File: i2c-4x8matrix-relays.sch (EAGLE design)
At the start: 83 parts, among them IC1 MCP23008/SS, IC2 MCP23008/SS, IC3 MCP23008/SS, IC4 MCP23008/SS, IC5 TBD62083AFNG, IC6 TBD62083AFNG, IC7 TBD62083AFNG, IC8 TBD62083AFNG

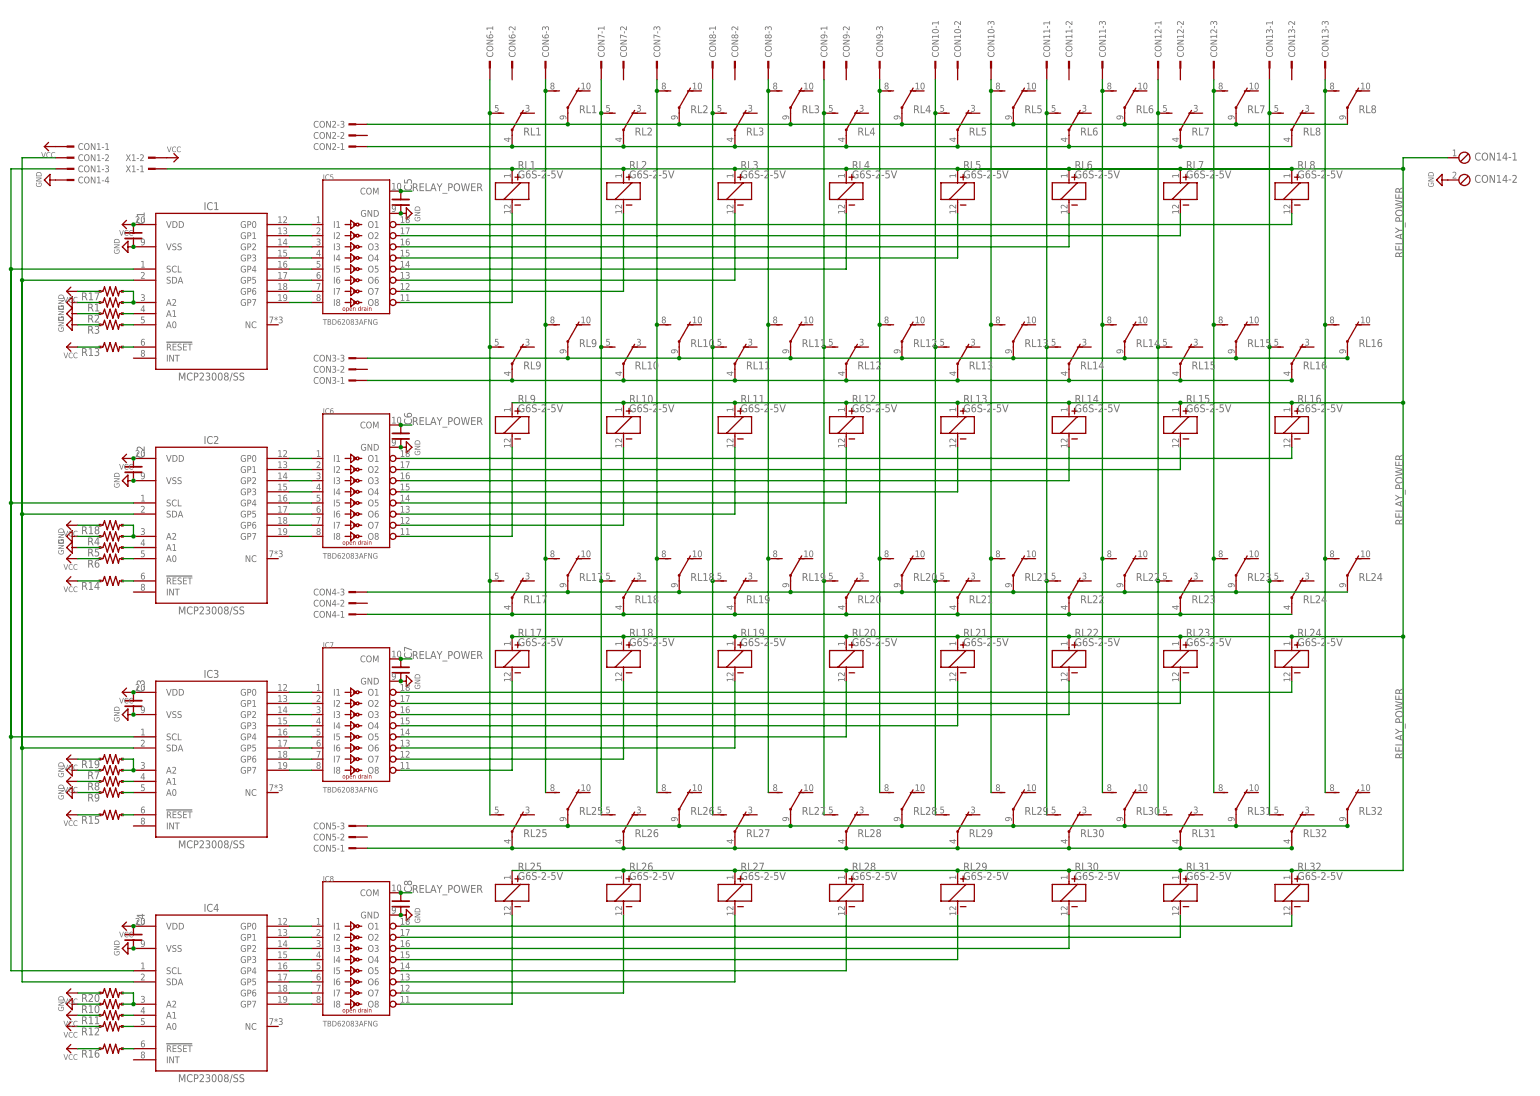
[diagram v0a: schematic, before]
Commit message: update schematic and layout to use PCA9XXX IO expander
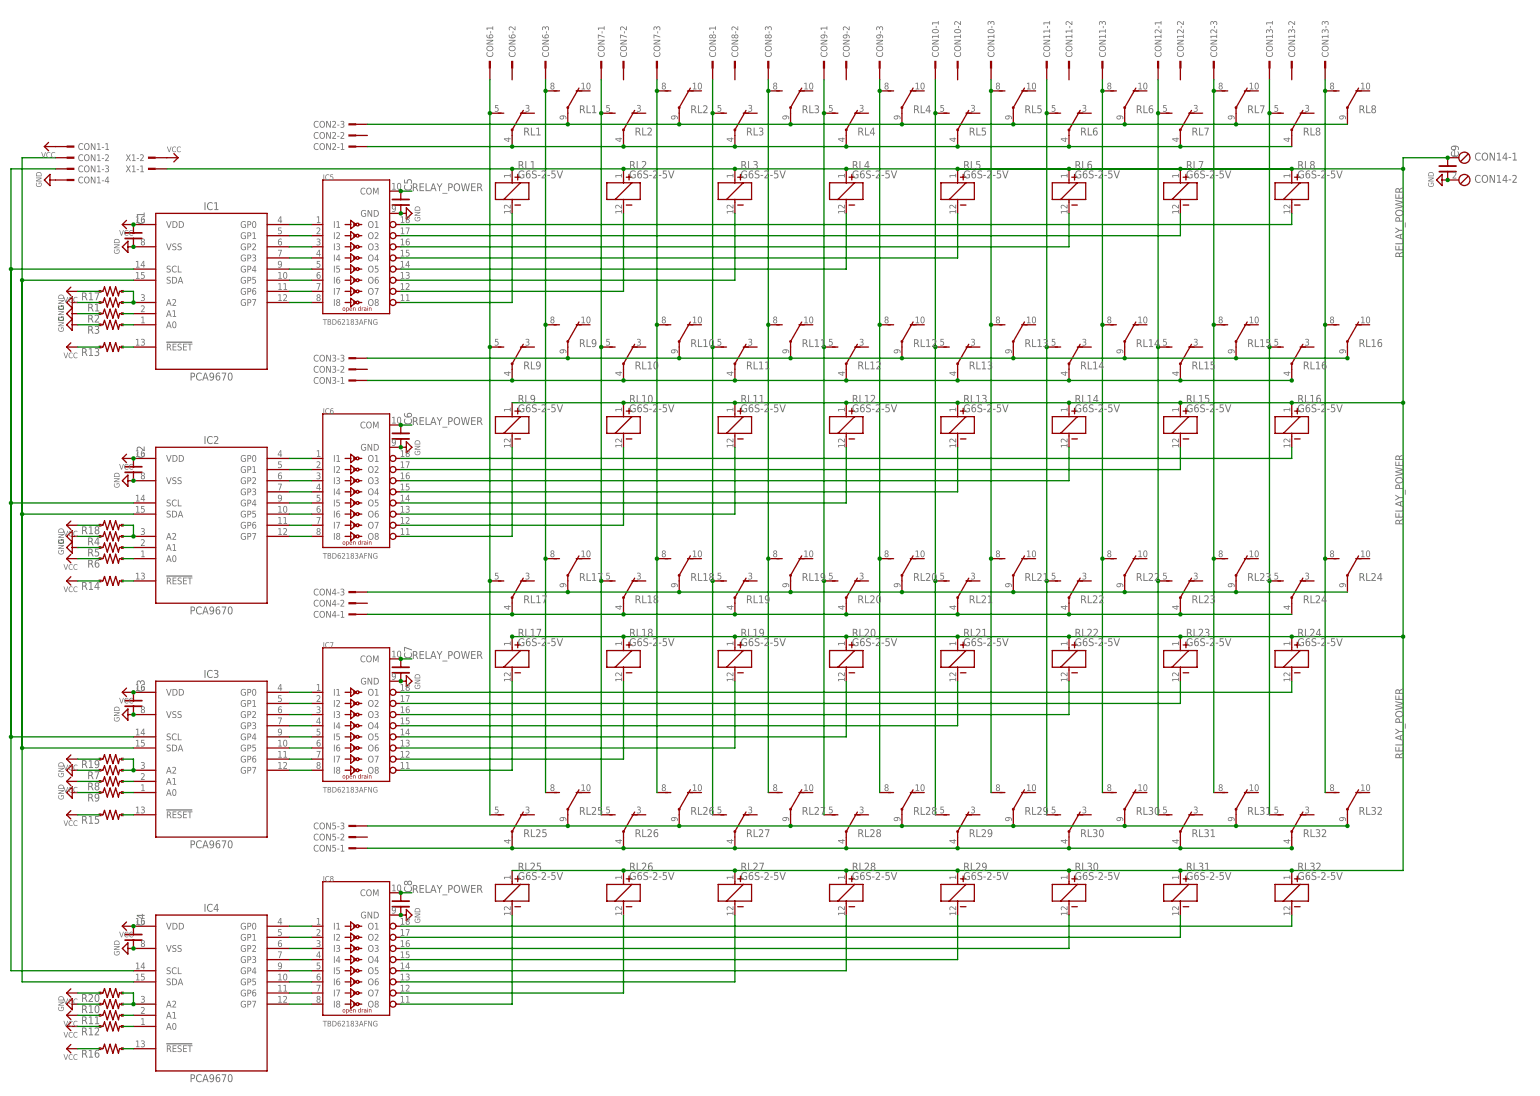
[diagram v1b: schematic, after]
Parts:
- added C9: (no value), mylib:C-SMD-10U-1608
- IC1, IC2, IC3, IC4: value MCP23008/SS -> PCA9670; device mylib:MCP23008/SS -> mylib:PCA9670
- IC5, IC6, IC7, IC8: value TBD62083AFNG -> TBD62183AFNG; device mylib:TBD62083AFNG -> mylib:TBD62183AFNG
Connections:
- net GND: now also C9.2
- net RELAY_POWER: now also C9.1
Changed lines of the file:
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@@
 <part name="RL15" library="mylib" deviceset="G6S-2-*" device="" technology="5V"/>
 <part name="RL16" library="mylib" deviceset="G6S-2-*" device="" technology="5V"/>
-<part name="IC5" library="mylib" deviceset="TBD62083A" device="FNG" value="TBD62083AFNG"/>
-<part name="IC6" library="mylib" deviceset="TBD62083A" device="FNG" value="TBD62083AFNG"/>
+<part name="IC5" library="mylib" deviceset="TBD62183A" device="FNG" value="TBD62183AFNG"/>
+<part name="IC6" library="mylib" deviceset="TBD62183A" device="FNG" value="TBD62183AFNG"/>
 <part name="RL17" library="mylib" deviceset="G6S-2-*" device="" technology="5V"/>
 <part name="RL18" library="mylib" deviceset="G6S-2-*" device="" technology="5V"/>
@@
 <part name="RL31" library="mylib" deviceset="G6S-2-*" device="" technology="5V"/>
 <part name="RL32" library="mylib" deviceset="G6S-2-*" device="" technology="5V"/>
-<part name="IC7" library="mylib" deviceset="TBD62083A" device="FNG" value="TBD62083AFNG"/>
-<part name="IC8" library="mylib" deviceset="TBD62083A" device="FNG" value="TBD62083AFNG"/>
-<part name="IC1" library="mylib" deviceset="MCP23008" device="/SS" value="MCP23008/SS"/>
-<part name="IC2" library="mylib" deviceset="MCP23008" device="/SS" value="MCP23008/SS"/>
-<part name="IC3" library="mylib" deviceset="MCP23008" device="/SS" value="MCP23008/SS"/>
-<part name="IC4" library="mylib" deviceset="MCP23008" device="/SS" value="MCP23008/SS"/>
+<part name="IC7" library="mylib" deviceset="TBD62183A" device="FNG" value="TBD62183AFNG"/>
+<part name="IC8" library="mylib" deviceset="TBD62183A" device="FNG" value="TBD62183AFNG"/>
+<part name="IC1" library="mylib" deviceset="PCA9670" device="" value="PCA9670"/>
+<part name="IC2" library="mylib" deviceset="PCA9670" device="" value="PCA9670"/>
+<part name="IC3" library="mylib" deviceset="PCA9670" device="" value="PCA9670"/>
+<part name="IC4" library="mylib" deviceset="PCA9670" device="" value="PCA9670"/>
 <part name="SUPPLY1" library="mylib" deviceset="GND" device=""/>
 <part name="SUPPLY2" library="mylib" deviceset="GND" device=""/>
@@
 <part name="X1" library="mylib" deviceset="PH-1X2SG" device=""/>
 <part name="P+18" library="mylib" deviceset="VCC" device=""/>
+<part name="C9" library="mylib" deviceset="C-SMD-*" device="-1608" technology="10U"/>
 </parts>
 <sheets>
@@
 <instance part="X1" gate="-2" x="60.96" y="215.9" rot="R180"/>
 <instance part="P+18" gate="VCC" x="66.04" y="215.9" rot="R270"/>
+<instance part="C9" gate="G$1" x="355.6" y="213.36"/>
 </instances>
 <busses>
@@
 <pinref part="CON14" gate="-2" pin="1"/>
 <pinref part="SUPPLY18" gate="GND" pin="GND"/>
+<pinref part="C9" gate="G$1" pin="2"/>
+<junction x="355.6" y="210.82"/>
+<pinref part="C9" gate="G$1" pin="2"/>
 </segment>
 </net>
@@
 <pinref part="X1" gate="-1" pin="1"/>
 <wire x1="142.24" y1="213.36" x2="63.5" y2="213.36" width="0.1524" layer="91"/>
-</segment>
-<segment>
+<pinref part="C9" gate="G$1" pin="1"/>
+<junction x="355.6" y="215.9"/>
+</segment>
+<segment>
